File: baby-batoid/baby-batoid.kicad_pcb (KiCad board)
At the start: 2 copper layers, 20.3 x 50.8 mm, 23 parts, among them J1 USB_C_Receptacle_USB2.0, J2 Conn_01x20, J3 Conn_01x20, U1 STM32F072CBT6, U2 PRTR5V0U2X, U3 XC6206PxxxMR-Regulator_Linear

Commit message: built baby batoid :D
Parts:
- removed J2, J3: Conn_01x20, Connector_PinHeader_2.54mm:PinHeader_1x20_P2.54mm_Vertical
- added D1: D_Small, Diode_SMD:D_SOD-123, B.Cu at (85.6, 58.9)
- added D10: D_Small, Diode_SMD:D_SOD-123, B.Cu at (93.0, 99.0)
- added D11: D_Small, Diode_SMD:D_SOD-123, B.Cu at (111.7, 102.3)
- added D12: D_Small, Diode_SMD:D_SOD-123, B.Cu at (130.5, 105.7)
- added D13: D_Small, Diode_SMD:D_SOD-123, B.Cu at (149.2, 109.0)
- added D14: D_Small, Diode_SMD:D_SOD-123, B.Cu at (73.2, 114.8)
- added D15: D_Small, Diode_SMD:D_SOD-123, B.Cu at (127.1, 124.4)
- added D16: D_Small, Diode_SMD:D_SOD-123, B.Cu at (168.4, 59.3)
- added D17: D_Small, Diode_SMD:D_SOD-123, B.Cu at (193.9, 65.0)
- added D18: D_Small, Diode_SMD:D_SOD-123, B.Cu at (212.6, 61.7)
- added D19: D_Small, Diode_SMD:D_SOD-123, B.Cu at (231.4, 58.5)
- added D2: D_Small, Diode_SMD:D_SOD-123, B.Cu at (104.4, 62.3)
- added D20: D_Small, Diode_SMD:D_SOD-123, B.Cu at (183.0, 86.2)
- added D21: D_Small, Diode_SMD:D_SOD-123, B.Cu at (201.8, 83.0)
- added D22: D_Small, Diode_SMD:D_SOD-123, B.Cu at (220.6, 79.7)
- added D23: D_Small, Diode_SMD:D_SOD-123, B.Cu at (239.3, 76.4)
- added D24: D_Small, Diode_SMD:D_SOD-123, B.Cu at (195.7, 103.3)
- added D25: D_Small, Diode_SMD:D_SOD-123, B.Cu at (214.4, 100.1)
- added D26: D_Small, Diode_SMD:D_SOD-123, B.Cu at (233.2, 96.8)
- added D27: D_Small, Diode_SMD:D_SOD-123, B.Cu at (252.0, 93.6)
- added D28: D_Small, Diode_SMD:D_SOD-123, B.Cu at (196.6, 122.5)
- added D29: D_Small, Diode_SMD:D_SOD-123, B.Cu at (245.9, 114.0)
- added D3: D_Small, Diode_SMD:D_SOD-123, B.Cu at (123.1, 65.7)
- added D4: D_Small, Diode_SMD:D_SOD-123, B.Cu at (141.9, 69.0)
- added D5: D_Small, Diode_SMD:D_SOD-123, B.Cu at (79.9, 77.3)
- added D6: D_Small, Diode_SMD:D_SOD-123, B.Cu at (105.7, 81.9)
- added D7: D_Small, Diode_SMD:D_SOD-123, B.Cu at (124.5, 85.3)
- added D8: D_Small, Diode_SMD:D_SOD-123, B.Cu at (143.2, 88.6)
- added D9: D_Small, Diode_SMD:D_SOD-123, B.Cu at (69.5, 94.8)
- added MX1: MX_SW_HS, marbastlib-mx:SW_MX_HS_CPG151101S11_1u, B.Cu at (84.1, 53.6)
- added MX10: MX_SW_HS, marbastlib-mx:SW_MX_HS_CPG151101S11_1u, B.Cu at (91.4, 93.6)
- added MX11: MX_SW_HS, marbastlib-mx:SW_MX_HS_CPG151101S11_1u, B.Cu at (110.2, 97.0)
- added MX12: MX_SW_HS, marbastlib-mx:SW_MX_HS_CPG151101S11_1u, B.Cu at (128.9, 100.3)
- added MX13: MX_SW_HS, marbastlib-mx:SW_MX_HS_CPG151101S11_1u, B.Cu at (147.7, 103.7)
- added MX14: MX_SW_HS, marbastlib-mx:SW_MX_HS_CPG151101S11_1u, B.Cu at (71.6, 109.4)
- added MX15: MX_SW_HS, marbastlib-mx:SW_MX_HS_CPG151101S11_1u, B.Cu at (125.5, 119.1)
- added MX16: MX_SW_HS, marbastlib-mx:SW_MX_HS_CPG151101S11_1u, B.Cu at (171.8, 63.8)
- added MX17: MX_SW_HS, marbastlib-mx:SW_MX_HS_CPG151101S11_1u, B.Cu at (190.5, 60.5)
- added MX18: MX_SW_HS, marbastlib-mx:SW_MX_HS_CPG151101S11_1u, B.Cu at (209.3, 57.2)
- added MX19: MX_SW_HS, marbastlib-mx:SW_MX_HS_CPG151101S11_1u, B.Cu at (228.1, 54.0)
- added MX2: MX_SW_HS, marbastlib-mx:SW_MX_HS_CPG151101S11_1u, B.Cu at (102.8, 56.9)
- added MX20: MX_SW_HS, marbastlib-mx:SW_MX_HS_CPG151101S11_1u, B.Cu at (179.7, 81.7)
- added MX21: MX_SW_HS, marbastlib-mx:SW_MX_HS_CPG151101S11_1u, B.Cu at (198.5, 78.5)
- added MX22: MX_SW_HS, marbastlib-mx:SW_MX_HS_CPG151101S11_1u, B.Cu at (217.3, 75.2)
- added MX23: MX_SW_HS, marbastlib-mx:SW_MX_HS_CPG151101S11_1u, B.Cu at (236.0, 71.9)
- added MX24: MX_SW_HS, marbastlib-mx:SW_MX_HS_CPG151101S11_1u, B.Cu at (192.4, 98.8)
- added MX25: MX_SW_HS, marbastlib-mx:SW_MX_HS_CPG151101S11_1u, B.Cu at (211.1, 95.6)
- added MX26: MX_SW_HS, marbastlib-mx:SW_MX_HS_CPG151101S11_1u, B.Cu at (229.9, 92.3)
- added MX27: MX_SW_HS, marbastlib-mx:SW_MX_HS_CPG151101S11_1u, B.Cu at (248.7, 89.1)
- added MX28: MX_SW_HS, marbastlib-mx:SW_MX_HS_CPG151101S11_1u, B.Cu at (193.3, 118.0)
- added MX29: MX_SW_HS, marbastlib-mx:SW_MX_HS_CPG151101S11_1u, B.Cu at (242.5, 109.5)
- added MX3: MX_SW_HS, marbastlib-mx:SW_MX_HS_CPG151101S11_1u, B.Cu at (121.6, 60.3)
- added MX4: MX_SW_HS, marbastlib-mx:SW_MX_HS_CPG151101S11_1u, B.Cu at (140.3, 63.7)
- added MX5: MX_SW_HS, marbastlib-mx:SW_MX_HS_CPG151101S11_1u, B.Cu at (78.4, 71.9)
- added MX6: MX_SW_HS, marbastlib-mx:SW_MX_HS_CPG151101S11_1u, B.Cu at (104.1, 76.5)
- added MX7: MX_SW_HS, marbastlib-mx:SW_MX_HS_CPG151101S11_1u, B.Cu at (122.9, 79.9)
- added MX8: MX_SW_HS, marbastlib-mx:SW_MX_HS_CPG151101S11_1u, B.Cu at (141.6, 83.3)
- added MX9: MX_SW_HS, marbastlib-mx:SW_MX_HS_CPG151101S11_1u, B.Cu at (68.0, 89.4)
- BOOT1, C1, C10, C2, C3, C4, C5, C6, C7, C8, C9, F1, J1, R1, R2, R3, R4, RST1, U1, U2, U3: moved to B.Cu
- moved C5 45.1 mm to (175.4, 105.7), turned to -80.16 degrees
- moved C6 44.4 mm to (175.2, 107.3), turned to 9.84 degrees
- moved BOOT1 44.3 mm to (176.1, 118.5), turned to -80.16 degrees
- moved C3 43.2 mm to (173.7, 97.1), turned to 9.84 degrees
- moved R3 39.9 mm to (173.2, 111.9), turned to -170.16 degrees
- moved C2 38.7 mm to (161.3, 61.1), turned to -0.16 degrees
- moved U3 36.7 mm to (160.1, 58.4), turned to 179.84 degrees
- moved U1 35.9 mm to (170.3, 102.3), turned to 99.84 degrees
- moved R4 35.2 mm to (170.8, 112.4), turned to -170.16 degrees
- moved R2 34.9 mm to (158.8, 49.6), turned to -0.16 degrees
- moved R1 34.8 mm to (158.8, 52.1), turned to 179.84 degrees
- moved C8 34.8 mm to (158.8, 54.1), turned to 89.84 degrees
- moved C10 34.5 mm to (158.6, 60.9), turned to 179.84 degrees
- moved C1 34.4 mm to (170.1, 110.2), turned to -170.16 degrees
- moved C7 34.2 mm to (169.9, 109.0), turned to 9.84 degrees
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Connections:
- U1 pad 10: /A0 -> ROW3
- U1 pad 11: /A1 -> ROW2
- U1 pad 19: /B1 -> COL0
- U1 pad 20: /B2 -> COL1
- U1 pad 21: /B10 -> COL2
- U1 pad 22: /B11 -> COL3
- U1 pad 25: /B12 -> ROW0
- U1 pad 26: /B13 -> ROW1
- U1 pad 37: /A14 -> COL4
- U1 pad 38: /A15 -> COL5
- U1 pad 39: /B3 -> COL6
- U1 pad 40: /B4 -> COL7
- U2 pad 2: D_N -> D-
- U2 pad 3: D_P -> D+
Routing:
- net ROW2: track 0.00 -> 241.5 mm
- net ROW3: track 0.00 -> 223.7 mm, vias 0 -> 2
- net ROW0: track 0.00 -> 204.7 mm, vias 0 -> 3
- net ROW1: track 0.00 -> 185.0 mm, vias 0 -> 2
- net COL7: track 0.00 -> 180.4 mm
- net COL0: track 0.00 -> 167.2 mm, vias 0 -> 3
- net COL1: track 0.00 -> 138.3 mm, vias 0 -> 3
- net COL2: track 0.00 -> 123.2 mm, vias 0 -> 1
- net COL6: track 0.00 -> 98.2 mm
- net COL3: track 0.00 -> 94.5 mm, vias 0 -> 1
- net COL5: track 0.00 -> 79.0 mm
- net COL4: track 0.00 -> 67.4 mm
- net D+: track 0.00 -> 61.2 mm
- net Net-(D28-K): track 0.00 -> 59.9 mm
- net Net-(D7-K): track 0.00 -> 59.9 mm
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- added copper zone on B.Cu, net GND
- added copper zone on F.Cu, net GND
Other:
- board size 20.3 x 50.8 mm -> 209.4 x 93.7 mm
- board text added: "baby batoid"
- board text added: "by newx inspired by Kotte's batoid"

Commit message: production file work
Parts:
- added REF**: MountingHole_2.2mm_M2, MountingHole:MountingHole_2.2mm_M2, F.Cu at (66.2, 47.1)
- added REF**: MountingHole_2.2mm_M2, MountingHole:MountingHole_2.2mm_M2, F.Cu at (55.1, 103.4)
- added REF**: MountingHole_2.2mm_M2, MountingHole:MountingHole_2.2mm_M2, F.Cu at (155.4, 125.6)
- added REF**: MountingHole_2.2mm_M2, MountingHole:MountingHole_2.2mm_M2, F.Cu at (145.5, 40.3)
- added REF**: MountingHole_2.2mm_M2, MountingHole:MountingHole_2.2mm_M2, F.Cu at (243.3, 47.6)
- added REF**: MountingHole_2.2mm_M2, MountingHole:MountingHole_2.2mm_M2, F.Cu at (255.3, 103.6)
- added REF**: MountingHole_2.2mm_M2, MountingHole:MountingHole_2.2mm_M2, F.Cu at (165.7, 40.4)
- MX5: footprint marbastlib-mx:SW_MX_HS_CPG151101S11_1u -> marbastlib-mx:SW_MX_HS_CPG151101S11_1.75u
- MX9: footprint marbastlib-mx:SW_MX_HS_CPG151101S11_1u -> marbastlib-mx:SW_MX_HS_CPG151101S11_1.5u
- moved D18 3.83 mm to (211.3, 58.2)
- moved C6 3.83 mm to (173.9, 103.7)
- moved MX23 3.83 mm to (234.7, 68.4)
- moved MX28 3.83 mm to (191.9, 114.4)
- moved D21 3.83 mm to (200.5, 79.4)
- moved D27 3.83 mm to (250.6, 90.0)
- moved MX11 3.83 mm to (108.8, 93.4)
- moved MX19 3.83 mm to (226.7, 50.4)
- moved D29 3.83 mm to (244.5, 110.4)
- moved MX15 3.83 mm to (124.2, 115.5)
- moved D3 3.83 mm to (121.8, 62.1)
- moved MX13 3.83 mm to (146.3, 100.1)
- moved MX14 3.83 mm to (70.3, 105.8)
- moved BOOT1 3.83 mm to (174.8, 115.0)
- moved MX29 3.83 mm to (241.2, 105.9)
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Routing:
- net ROW2: track 241.5 -> 232.8 mm
- net ROW3: track 223.7 -> 217.9 mm
- net COL7: track 180.4 -> 179.2 mm
- net GND: track 196.5 -> 197.1 mm
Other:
- board size 209.4 x 93.7 mm -> 214.1 x 94.1 mm

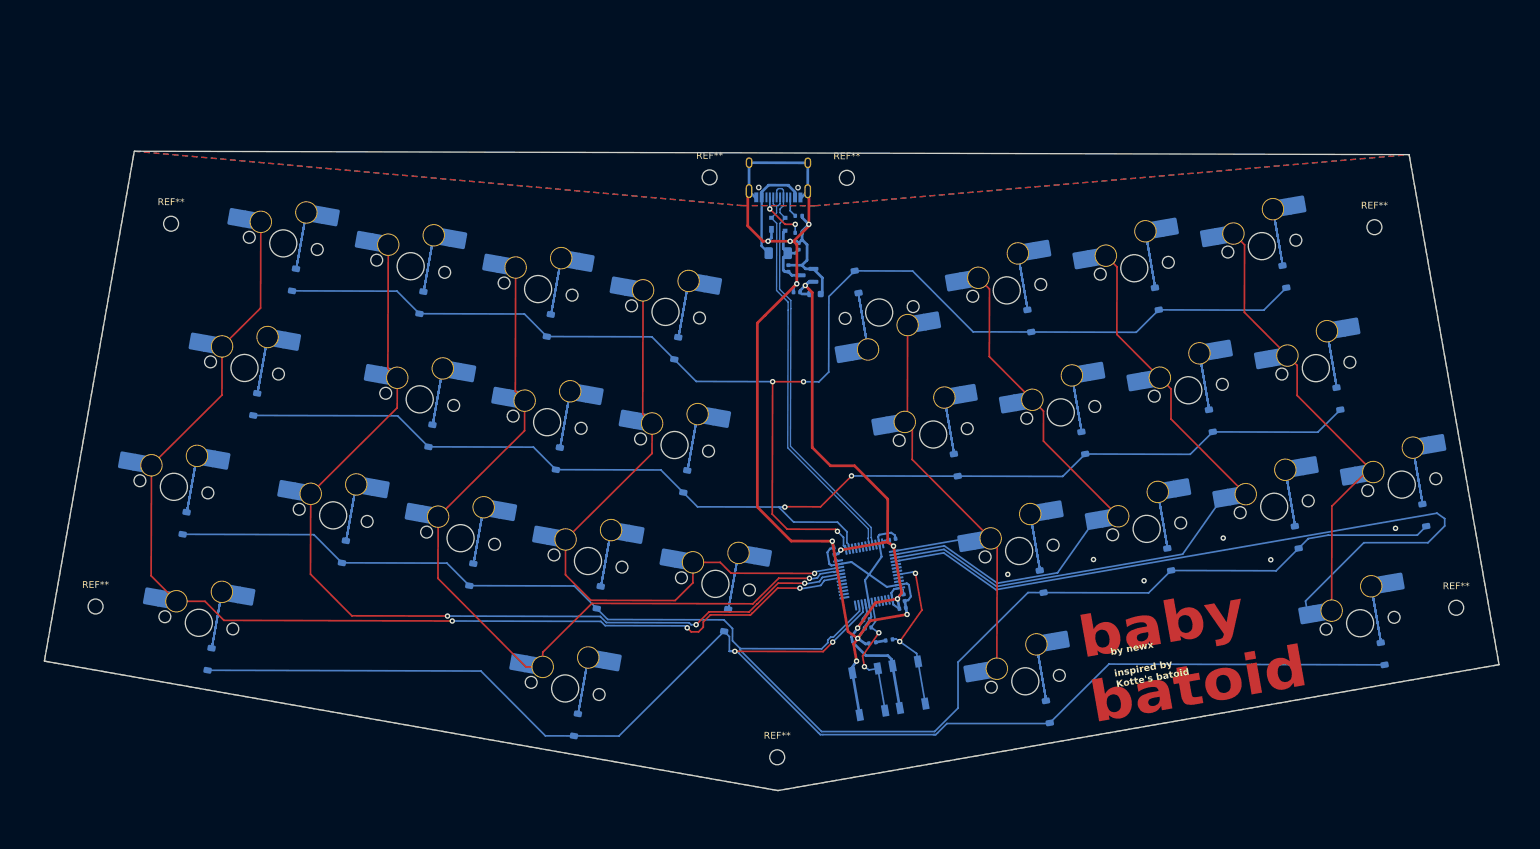
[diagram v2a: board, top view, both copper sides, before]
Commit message: cleaned up left routing, need to do right still
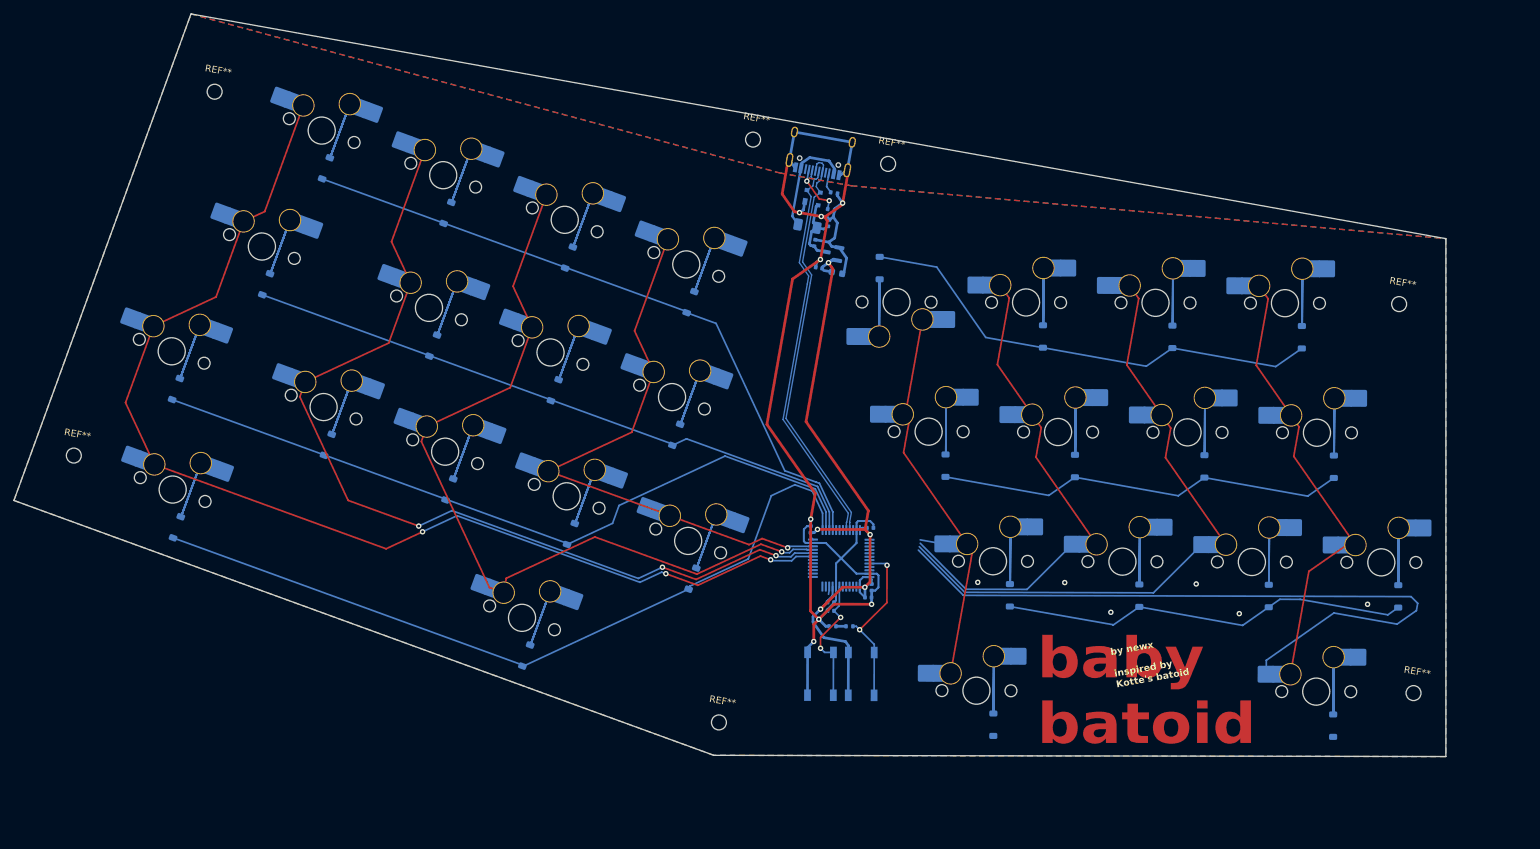
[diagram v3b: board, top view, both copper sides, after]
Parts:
- moved REF** 22.4 mm to (51.9, 81.2), turned to -10 degrees
- moved REF** 20.5 mm to (72.6, 27.7), turned to -10 degrees
- moved D14 20.0 mm to (67.1, 91.8), turned to -110.16 degrees
- moved MX14 20.0 mm to (66.4, 86.2), turned to 159.84 degrees
- moved MX9 19.9 mm to (66.3, 65.9), turned to 159.84 degrees
- moved D9 19.8 mm to (66.9, 71.4), turned to -110.16 degrees
- moved MX5 18.1 mm to (79.6, 50.5), turned to 159.84 degrees
- moved D5 17.8 mm to (80.2, 56.0), turned to -110.16 degrees
- moved MX1 17.5 mm to (88.4, 33.4), turned to 159.84 degrees
- moved D1 17.1 mm to (89.0, 38.9), turned to -110.16 degrees
- moved MX10 16.0 mm to (88.7, 74.1), turned to 159.84 degrees
- moved D10 15.9 mm to (89.3, 79.6), turned to -110.16 degrees
- moved MX2 14.2 mm to (106.3, 40.0), turned to 159.84 degrees
- moved REF** 14.0 mm to (249.0, 116.2), turned to -10 degrees
- moved D2 13.8 mm to (106.9, 45.5), turned to -110.16 degrees
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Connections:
- D16 pad 2: ROW0 -> ROW4
- D17 pad 2: ROW0 -> ROW4
- D18 pad 2: ROW0 -> ROW4
- D19 pad 2: ROW0 -> ROW4
- D20 pad 2: ROW1 -> ROW5
- D21 pad 2: ROW1 -> ROW5
- D22 pad 2: ROW1 -> ROW5
- D23 pad 2: ROW1 -> ROW5
- D24 pad 2: ROW2 -> ROW6
- D25 pad 2: ROW2 -> ROW6
- D26 pad 2: ROW2 -> ROW6
- D27 pad 2: ROW2 -> ROW6
- D28 pad 2: ROW3 -> ROW7
- D29 pad 2: ROW3 -> ROW7
- U1 pad 10: ROW3 -> /A0
- U1 pad 11: ROW2 -> /A1
- U1 pad 25: ROW0 -> ROW3
- U1 pad 26: ROW1 -> ROW2
- U1 pad 27: /B14 -> ROW1
- U1 pad 28: /B15 -> ROW0
- U1 pad 37: COL4 -> /A14
- U1 pad 38: COL5 -> /A15
- U1 pad 39: COL6 -> /B3
- U1 pad 40: COL7 -> /B4
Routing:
- net ROW2: track 232.8 -> 109.9 mm
- net ROW0: track 204.7 -> 98.5 mm, vias 3 -> 0
- net ROW3: track 217.9 -> 114.3 mm, vias 2 -> 0
- net ROW1: track 185.0 -> 94.0 mm, vias 2 -> 0
- net ROW4: track 0.00 -> 70.0 mm
- net ROW5: track 0.00 -> 60.4 mm
- net ROW6: track 0.00 -> 60.2 mm
- net COL3: track 94.5 -> 85.4 mm
- net COL5: track 79.0 -> 71.6 mm
- net COL6: track 98.2 -> 90.9 mm
- net COL7: track 179.2 -> 172.0 mm
- net COL4: track 67.4 -> 60.6 mm
- net GND: track 197.1 -> 191.8 mm
- net +3V3: track 107.1 -> 105.0 mm
- net COL1: track 138.3 -> 136.6 mm
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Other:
- board size 214.1 x 94.1 mm -> 210.7 x 109.3 mm

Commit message: finished cleaning routing up
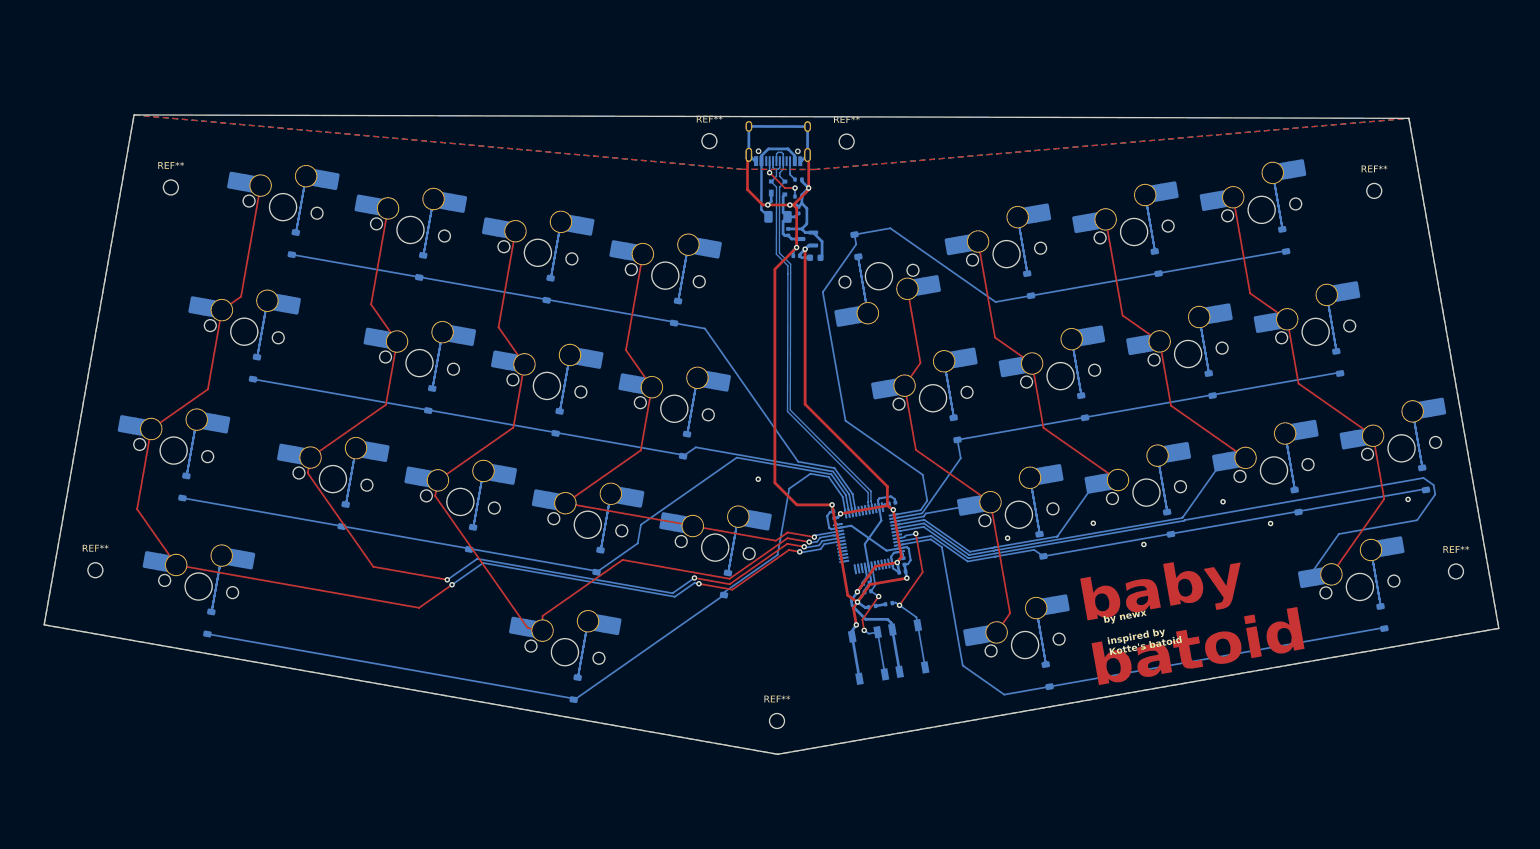
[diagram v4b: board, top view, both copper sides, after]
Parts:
- moved REF** 19.0 mm to (255.3, 98.3), turned to 0 degrees
- moved D27 17.7 mm to (250.6, 84.7), turned to -80.16 degrees
- moved D29 17.5 mm to (244.5, 105.1), turned to -80.16 degrees
- moved REF** 17.2 mm to (55.1, 98.1), turned to 0 degrees
- moved REF** 17.1 mm to (243.3, 42.3), turned to 0 degrees
- moved MX27 17.0 mm to (247.3, 80.2), turned to -170.16 degrees
- moved MX29 16.7 mm to (241.2, 100.6), turned to -170.16 degrees
- moved REF** 15.5 mm to (66.2, 41.8), turned to 0 degrees
- moved D23 15.4 mm to (238.0, 67.5), turned to -80.16 degrees
- moved D14 14.9 mm to (71.8, 105.9), turned to -100.16 degrees
- moved MX23 14.8 mm to (234.6, 63.0), turned to -170.16 degrees
- moved MX14 14.8 mm to (70.3, 100.5), turned to 169.84 degrees
- moved MX9 14.6 mm to (66.6, 80.5), turned to 169.84 degrees
- moved D26 14.6 mm to (231.8, 87.9), turned to -80.16 degrees
- moved D19 14.5 mm to (230.0, 49.6), turned to -80.16 degrees
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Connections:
- U1 pad 37: /A14 -> ROW4
- U1 pad 38: /A15 -> ROW5
- U1 pad 39: /B3 -> COL4
- U1 pad 40: /B4 -> COL5
- U1 pad 41: /B5 -> COL6
- U1 pad 42: /B6 -> COL7
- U1 pad 45: /B8 -> ROW6
- U1 pad 46: /B9 -> ROW7
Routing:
- net ROW7: track 0.00 -> 88.6 mm
- net ROW4: track 70.0 -> 120.3 mm
- net Net-(D28-K): track 59.9 -> 32.7 mm
- net Net-(D9-K): track 59.9 -> 32.7 mm
- net Net-(D21-K): track 59.9 -> 32.7 mm
- net Net-(D8-K): track 59.9 -> 32.7 mm
- net Net-(D7-K): track 59.9 -> 32.7 mm
- net Net-(D17-K): track 59.9 -> 32.7 mm
- net Net-(D4-K): track 59.9 -> 32.7 mm
- net Net-(D11-K): track 59.9 -> 32.7 mm
- net Net-(D20-K): track 59.9 -> 32.7 mm
- net Net-(D1-K): track 59.9 -> 32.7 mm
- net Net-(D29-K): track 59.9 -> 32.7 mm
- net Net-(D26-K): track 59.9 -> 32.7 mm
- net Net-(D25-K): track 59.9 -> 32.7 mm
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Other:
- board size 210.7 x 109.3 mm -> 214.1 x 94.1 mm
